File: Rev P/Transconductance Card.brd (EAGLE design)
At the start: 162.8 x 125.9 mm, 87 parts, among them IC1 74LS07D, IC10 ASSR-1530, IC12 LT1991MS, IC3 ISC0316-SMD, IC4 OP484, IC5 TLC272D, IC6 74LS00D, IC8 7438, IC9 ASSR-1530, Q1 IRF9Z24NPbF, Q2 2N7000, U1 MCP1700T-3302E/TT, X1 H15MLE

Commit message: Made bypass capacitor-diode thing symmetrical
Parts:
- added C44, C46: 1n, resistor:C1206
- added C45, C47: 0.1u, resistor:C1210
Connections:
- net GND: now also C44.2, C45.2, C46.2, C47.2
- net N$16: now also C44.1
- net N$22: now also C45.1
- net N$30: now also C46.1
- net N$32: now also C47.1
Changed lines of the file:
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@@
 <attribute name="VALUE" x="66.95" y="22.35" size="1.27" layer="27"/>
+</element>
+<element name="C44" library="resistor" package="C1206" value="1n" x="-20.32" y="-8.89" smashed="yes">
+<attribute name="NAME" x="-21.59" y="-7.62" size="1.27" layer="25"/>
+<attribute name="VALUE" x="-21.59" y="-11.43" size="1.27" layer="27"/>
+</element>
+<element name="C45" library="resistor" library_urn="urn:adsk.eagle:library:348" package="C1210" package3d_urn="urn:adsk.eagle:package:23619/2" value="0.1u" x="-20.32" y="-16.51" smashed="yes">
+<attribute name="NAME" x="-22.225" y="-14.605" size="1.27" layer="25"/>
+<attribute name="VALUE" x="-22.225" y="-19.685" size="1.27" layer="27"/>
+</element>
+<element name="C46" library="resistor" package="C1206" value="1n" x="-20.32" y="-24.13" smashed="yes">
+<attribute name="NAME" x="-21.59" y="-22.86" size="1.27" layer="25"/>
+<attribute name="VALUE" x="-21.59" y="-26.67" size="1.27" layer="27"/>
+</element>
+<element name="C47" library="resistor" library_urn="urn:adsk.eagle:library:348" package="C1210" package3d_urn="urn:adsk.eagle:package:23619/2" value="0.1u" x="-20.32" y="-31.75" smashed="yes">
+<attribute name="NAME" x="-22.225" y="-29.845" size="1.27" layer="25"/>
+<attribute name="VALUE" x="-22.225" y="-34.925" size="1.27" layer="27"/>
 </element>
 </elements>
@@
 <contactref element="U$1" pad="5"/>
 <contactref element="U$1" pad="4"/>
+<contactref element="C44" pad="2"/>
+<contactref element="C45" pad="2"/>
+<contactref element="C46" pad="2"/>
+<contactref element="C47" pad="2"/>
 <wire x1="129.54" y1="97.79" x2="135.89" y2="97.79" width="0" layer="19" extent="1-1"/>
 <wire x1="129.54" y1="93.98" x2="129.54" y2="97.79" width="0" layer="19" extent="1-1"/>
@@
 <wire x1="93.98" y1="87.63" x2="99.06" y2="90.17" width="0" layer="19" extent="1-1"/>
 <wire x1="88.9" y1="90.17" x2="93.98" y2="87.63" width="0" layer="19" extent="1-1"/>
+<wire x1="16.51" y1="18.415" x2="15.24" y2="11.43" width="0" layer="19" extent="1-1"/>
+<wire x1="19.685" y1="22.86" x2="16.51" y2="18.415" width="0" layer="19" extent="1-1"/>
+<wire x1="16.38" y1="27.94" x2="16.8275" y2="24.4475" width="0" layer="19" extent="1-1"/>
+<wire x1="24.13" y1="19.05" x2="19.685" y2="22.86" width="0" layer="19" extent="1-1"/>
 <wire x1="135.89" y1="90.17" x2="129.54" y2="93.98" width="0" layer="19" extent="1-1"/>
 <wire x1="135.89" y1="83.82" x2="135.89" y2="90.17" width="0" layer="19" extent="1-1"/>
@@
 <wire x1="125.4252" y1="56.1848" x2="130.5052" y2="61.2648" width="0" layer="19" extent="1-1"/>
 <wire x1="31.75" y1="8.89" x2="27.94" y2="2.54" width="0" layer="19" extent="1-1"/>
+<wire x1="25.53" y1="36.83" x2="19.3048" y2="32.7" width="0" layer="19" extent="1-1"/>
+<wire x1="26.67" y1="41.91" x2="25.4" y2="39.37" width="0" layer="19" extent="1-1"/>
+<wire x1="26.8" y1="31.75" x2="25.53" y2="36.83" width="0" layer="19" extent="1-1"/>
+<wire x1="34.29" y1="30.35" x2="29.21" y2="31.75" width="0" layer="19" extent="1-1"/>
+<wire x1="40.64" y1="36.7" x2="38.1" y2="30.35" width="0" layer="19" extent="1-1"/>
+<wire x1="46.99" y1="27.94" x2="46.99" y2="35.56" width="0" layer="19" extent="1-1"/>
 <wire x1="67.31" y1="1.5875" x2="59.69" y2="1.5875" width="0" layer="19" extent="1-1"/>
 <wire x1="73.66" y1="1.5875" x2="67.31" y2="1.5875" width="0" layer="19" extent="1-1"/>
@@
 <wire x1="136.525" y1="1.5875" x2="130.81" y2="1.5875" width="0" layer="19" extent="1-1"/>
 <wire x1="100.2" y1="8.89" x2="106.55" y2="8.89" width="0" layer="19" extent="1-1"/>
-<wire x1="16.51" y1="30.48" x2="8.89" y2="30.48" width="0" layer="19" extent="1-1"/>
-<wire x1="16.8275" y1="24.4475" x2="16.38" y2="27.94" width="0" layer="19" extent="1-1"/>
-<wire x1="24.13" y1="19.05" x2="19.685" y2="22.86" width="0" layer="19" extent="1-1"/>
-<wire x1="25.53" y1="36.83" x2="19.3048" y2="32.7" width="0" layer="19" extent="1-1"/>
-<wire x1="26.67" y1="41.91" x2="25.4" y2="39.37" width="0" layer="19" extent="1-1"/>
-<wire x1="26.8" y1="31.75" x2="25.53" y2="36.83" width="0" layer="19" extent="1-1"/>
-<wire x1="34.29" y1="30.35" x2="29.21" y2="31.75" width="0" layer="19" extent="1-1"/>
-<wire x1="40.64" y1="36.7" x2="38.1" y2="30.35" width="0" layer="19" extent="1-1"/>
-<wire x1="46.99" y1="27.94" x2="46.99" y2="35.56" width="0" layer="19" extent="1-1"/>
 <wire x1="120.65" y1="10.16" x2="112.9" y2="8.89" width="0" layer="19" extent="1-1"/>
 <wire x1="53.975" y1="39.37" x2="46.99" y2="35.56" width="0" layer="19" extent="1-1"/>
@@
 <wire x1="60.96" y1="29.21" x2="57.15" y2="33.655" width="0" layer="19" extent="1-1"/>
 <wire x1="66.04" y1="27.94" x2="60.96" y2="29.21" width="0" layer="19" extent="1-1"/>
+<wire x1="67.65" y1="24.9" x2="66.04" y2="27.94" width="0" layer="19" extent="1-1"/>
+<wire x1="67.65" y1="24.4" x2="67.65" y2="24.9" width="0" layer="19" extent="1-1"/>
 <wire x1="69.85" y1="30.48" x2="66.04" y2="27.94" width="0" layer="19" extent="1-1"/>
 <wire x1="72.26" y1="34.29" x2="72.26" y2="30.48" width="0" layer="19" extent="1-1"/>
@@
 <wire x1="86.36" y1="27.94" x2="81.28" y2="26.67" width="0" layer="19" extent="1-1"/>
 <wire x1="93.98" y1="24.13" x2="88.9" y2="27.81" width="0" layer="19" extent="1-1"/>
+<wire x1="66.04" y1="15.24" x2="67.65" y2="24.4" width="0" layer="19" extent="1-1"/>
 <wire x1="104.14" y1="31.75" x2="97.79" y2="24.13" width="0" layer="19" extent="1-1"/>
 <wire x1="109.22" y1="30.48" x2="104.14" y2="31.75" width="0" layer="19" extent="1-1"/>
@@
 <wire x1="33.02" y1="67.31" x2="29.21" y2="64.9" width="0" layer="19" extent="1-1"/>
 <wire x1="41.91" y1="64.77" x2="33.02" y2="67.31" width="0" layer="19" extent="1-1"/>
-<wire x1="66.04" y1="15.24" x2="76.2" y2="13.97" width="0" layer="19" extent="1-1"/>
 <wire x1="53.34" y1="64.77" x2="41.91" y2="64.77" width="0" layer="19" extent="1-1"/>
 <wire x1="54.61" y1="54.61" x2="53.34" y2="64.77" width="0" layer="19" extent="1-1"/>
@@
 <wire x1="77.47" y1="54.61" x2="68.58" y2="54.74" width="0" layer="19" extent="1-1"/>
 <wire x1="76.1873" y1="73.152" x2="68.58" y2="64.77" width="0" layer="19" extent="1-1"/>
-<wire x1="16.51" y1="18.415" x2="2.54" y2="8.89" width="0" layer="19" extent="1-1"/>
-<wire x1="67.65" y1="24.9" x2="16.51" y2="18.415" width="0" layer="19" extent="1-1"/>
-<wire x1="67.65" y1="24.4" x2="67.65" y2="24.9" width="0" layer="19" extent="1-1"/>
+<wire x1="-18.92" y1="-8.89" x2="2.54" y2="8.89" width="0" layer="19" extent="1-1"/>
+<wire x1="-18.92" y1="-16.51" x2="-18.92" y2="-8.89" width="0" layer="19" extent="1-1"/>
+<wire x1="-18.92" y1="-24.13" x2="-18.92" y2="-16.51" width="0" layer="19" extent="1-1"/>
+<wire x1="-18.92" y1="-31.75" x2="-18.92" y2="-24.13" width="0" layer="19" extent="1-1"/>
 </signal>
 <signal name="+5V">
@@
 <wire x1="117.79" y1="88.73" x2="119.38" y2="90.32" width="1.016" layer="1"/>
 <wire x1="119.38" y1="90.32" x2="119.38" y2="91.31" width="1.016" layer="1"/>
+<contactref element="C44" pad="1"/>
+<wire x1="-21.72" y1="-8.89" x2="117.79" y2="88.73" width="0" layer="19" extent="1-1"/>
 </signal>
 <signal name="N$22">
@@
 <wire x1="115.89" y1="88.73" x2="115.57" y2="89.05" width="1.016" layer="1"/>
 <wire x1="115.57" y1="89.05" x2="115.57" y2="91.31" width="1.016" layer="1"/>
+<contactref element="C45" pad="1"/>
+<wire x1="-21.72" y1="-16.51" x2="115.89" y2="88.73" width="0" layer="19" extent="1-1"/>
 </signal>
 <signal name="N$30">
@@
 <wire x1="115.89" y1="76.37" x2="115.57" y2="76.05" width="1.016" layer="1"/>
 <wire x1="115.57" y1="76.05" x2="115.57" y2="73.79" width="1.016" layer="1"/>
+<contactref element="C46" pad="1"/>
+<wire x1="-21.72" y1="-24.13" x2="115.57" y2="73.79" width="0" layer="19" extent="1-1"/>
 </signal>
 <signal name="N$32">
@@
 <wire x1="117.79" y1="76.37" x2="119.38" y2="74.78" width="1.016" layer="1"/>
 <wire x1="119.38" y1="74.78" x2="119.38" y2="73.79" width="1.016" layer="1"/>
+<contactref element="C47" pad="1"/>
+<wire x1="-21.72" y1="-31.75" x2="119.38" y2="73.79" width="0" layer="19" extent="1-1"/>
 </signal>
 <signal name="N$33">

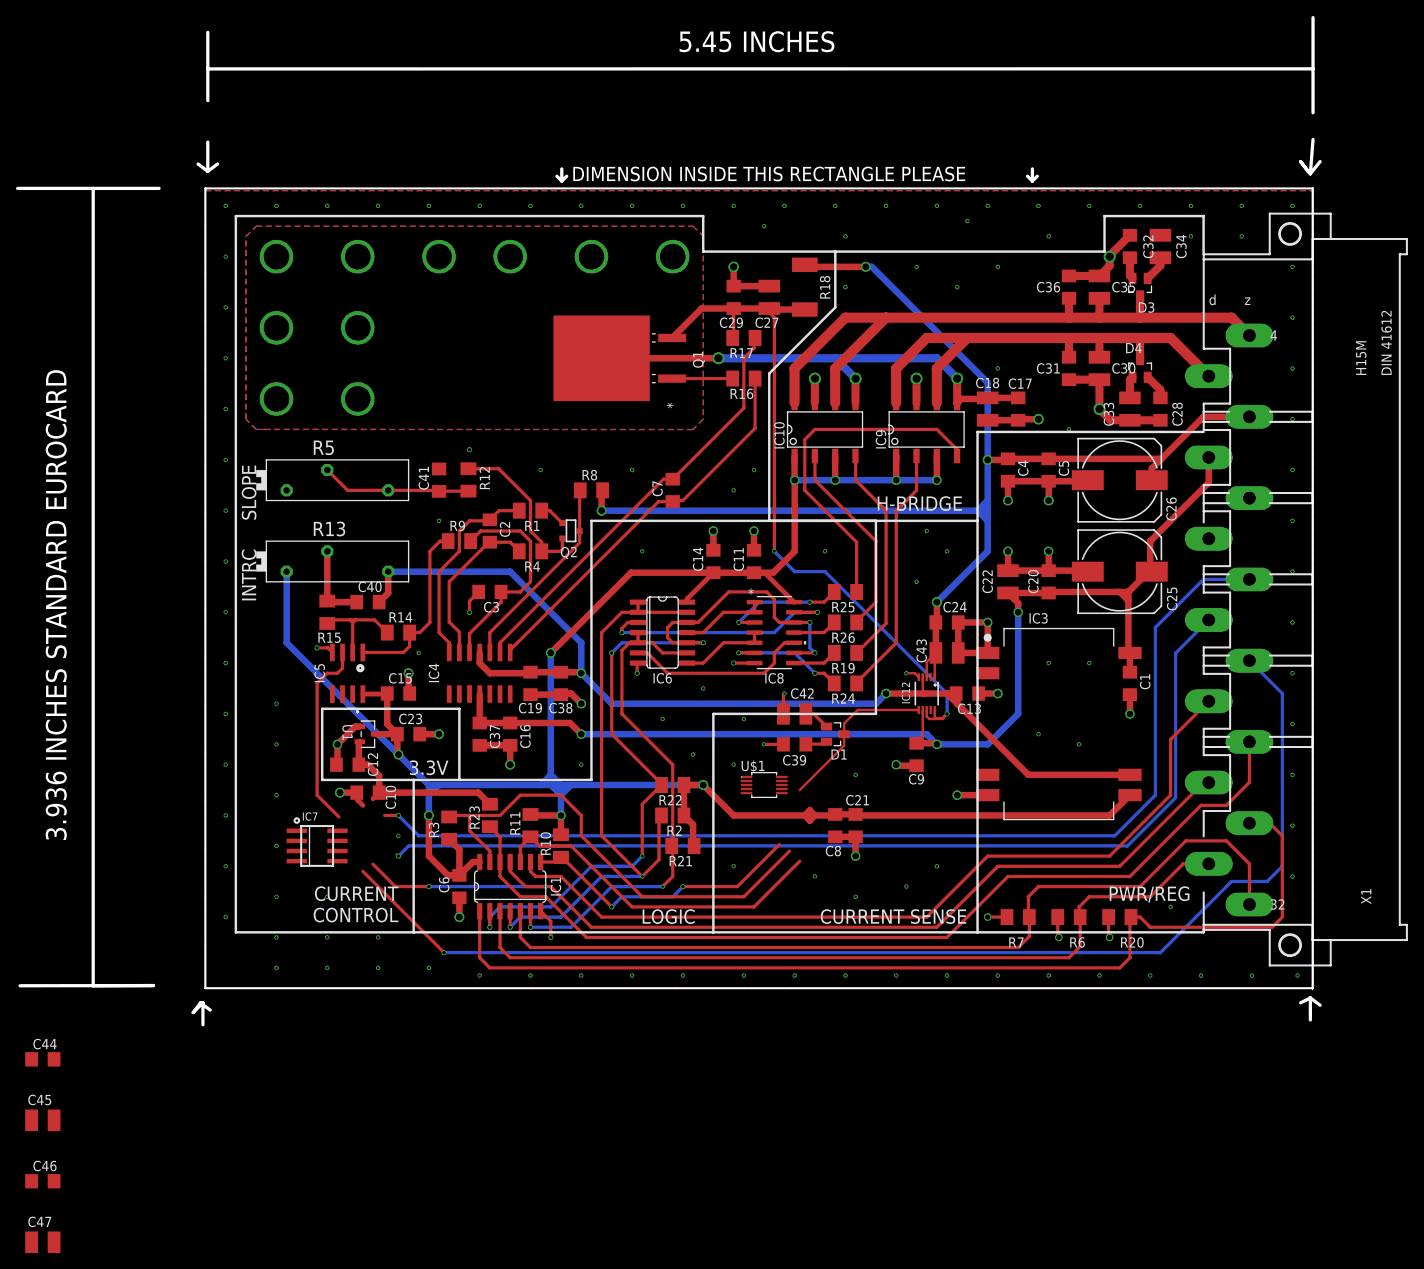
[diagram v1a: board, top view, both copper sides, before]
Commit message: Partial Board Routing
Need to finish routing power and update schematic power/GND symbols to be consistent with new convention
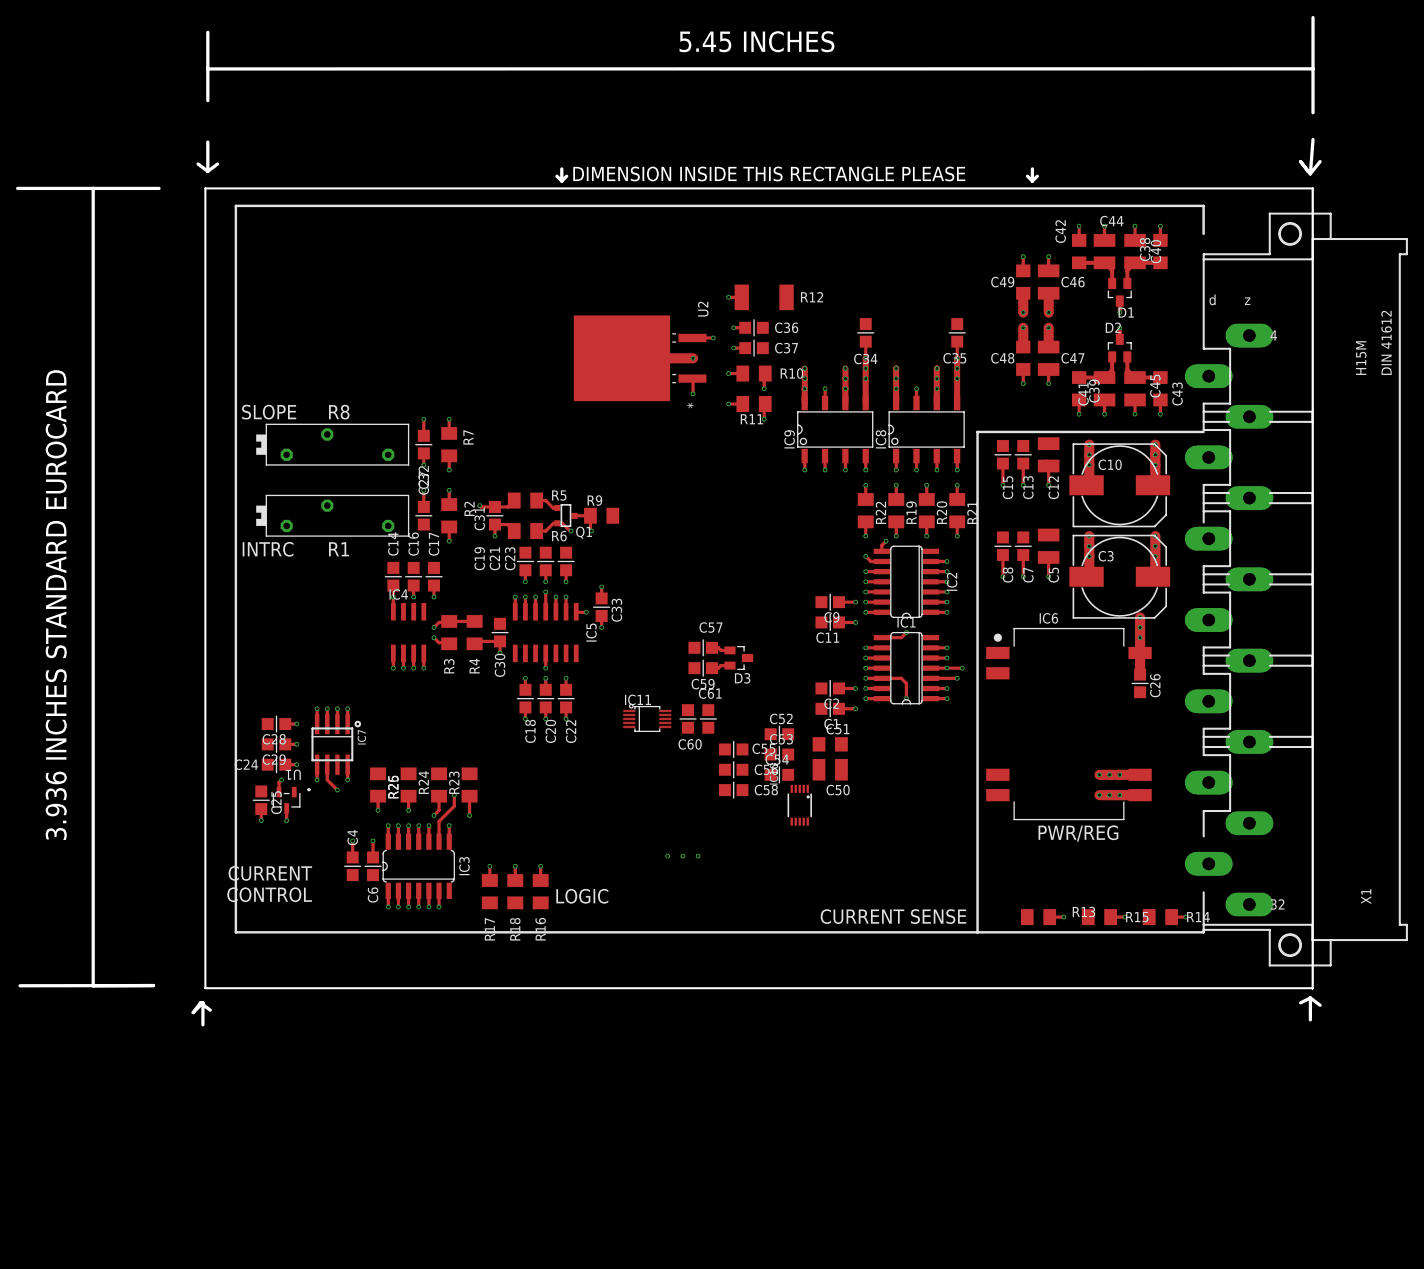
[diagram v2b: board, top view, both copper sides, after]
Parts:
- removed D4: BAS70-04, diode:SOT23
- removed IC12: LT1991MS, linear-technology:MSOP10
- removed Q2: 2N7000, UL_2N7002:SOT-23
- removed U$1: ADS8319, MeRCIS Lab Parts:VSSOP-10
- added C48, C49, C51: 1n, resistor:C1206
- added C50: 0.1u, resistor:C1210
- added C52, C55, C60: 1u, MeRCIS Lab Parts:C0805
- added C53, C56, C57, C61: 0.1u, MeRCIS Lab Parts:C0805
- added C54, C58: 0.01u, MeRCIS Lab Parts:C0805
- added C59: 1n, MeRCIS Lab Parts:C0805
- added D2: BAS70-04, diode:SOT23
- added IC11: ADS8319, MeRCIS Lab Parts:VSSOP-10
- added IC2: 74LS00, MeRCIS Lab Parts:74XX-US_SO14:1
- added U2: IRF9Z24NPbF, UL_IRF9Z24:D2PAK
- C1, C19: value 0.1u -> 1u; device resistor:C1206 -> MeRCIS Lab Parts:C0805
- C10, C3: value 0.1u -> 470u; device resistor:C1206 -> rcl:140CLH-1010
- C11, C14, C16, C20, C4: device resistor:C1206 -> MeRCIS Lab Parts:C0805
- C12: value 1u -> 10u; device resistor:C1206 -> resistor:C1210
- C13, C7, C9: value 0.01u -> 1u; device resistor:C1206 -> MeRCIS Lab Parts:C0805
- C15, C2, C21, C6: value 0.01u -> 0.1u; device resistor:C1206 -> MeRCIS Lab Parts:C0805
- C17, C24: value 1n -> 1u; device resistor:C1206 -> MeRCIS Lab Parts:C0805
- C18: value 0.1u -> 1u; device resistor:C1210 -> MeRCIS Lab Parts:C0805
- C22: value 10u -> 0.01u; device resistor:C1210 -> MeRCIS Lab Parts:C0805
- C23: value 1u -> 0.01u; device resistor:C1206 -> MeRCIS Lab Parts:C0805
- C25: value 470u -> 1u; device resistor1:153CLV-1010 -> MeRCIS Lab Parts:C0805
- C26: value 470u -> 0.1u; device resistor1:153CLV-1010 -> MeRCIS Lab Parts:C0805
- C27, C30, C34: device resistor:C1210 -> MeRCIS Lab Parts:C0805
- C28, C32, C36: value 1n -> 0.1u; device resistor:C1206 -> MeRCIS Lab Parts:C0805
- C29: value 1n -> 10u; device resistor:C1206 -> MeRCIS Lab Parts:C0805
- C31: value 1n -> 0.01u; device resistor:C1206 -> MeRCIS Lab Parts:C0805
- C33: value 0.1u -> 0.01u; device resistor:C1210 -> MeRCIS Lab Parts:C0805
- C35: value 0.1u -> 1n; device resistor:C1210 -> MeRCIS Lab Parts:C0805
- C37: value 0.01u -> 1n; device resistor:C1206 -> MeRCIS Lab Parts:C0805
- C38: value 0.01u -> 1n
- C40, C41: device resistor:C1206 -> resistor:C1210
- C42, C43: value 0.1u -> 1n; device resistor:C1210 -> resistor:C1206
- C44, C46: value 1n -> 0.1u; device resistor:C1206 -> resistor:C1210
- C5: value 0.1u -> 10u; device resistor:C1206 -> resistor:C1210
- C8: value 1u -> 0.1u; device resistor:C1206 -> MeRCIS Lab Parts:C0805
- IC1: value 74LS07D -> 74LS00; device 74xx-eu:SO14 -> MeRCIS Lab Parts:74XX-US_SO14:1
- IC10: value ASSR-1530 -> LT1991MS; device ASSR-1530:SO8 -> linear-technology:MSOP10
- IC3: value ISC0316-SMD -> 74LS07D; device SF_ISC03:SOP254P1879X863-16N -> 74xx-eu:SO14
- IC4: value OP484 -> TLC272D; device linear:SO14 -> linear:SO08
- IC5: value TLC272D -> OP484; device linear:SO08 -> linear:SO14
- IC6: value 74LS00D -> SF_ISC03_DC_DC16-SMD; device 74xx-us:SO14 -> MeRCIS Lab Parts:SF_ISC03_SOP254P1879X863-16N
- IC8: value 7438 -> ASSR-1530; device SN7438:D14 -> MeRCIS Lab Parts:ASSR-1530_SO8
- IC9: device ASSR-1530:SO8 -> MeRCIS Lab Parts:ASSR-1530_SO8
- Q1: value IRF9Z24NPbF -> 2N7000; device UL_IRF9Z24:D2PAK -> UL_2N7002:SOT-23
- R1: value 100ohm -> 20k; device resistor:M1206 -> rcl:PT-SPIN
- R10, R25: value 330 -> 1k
- R11: value 330 -> 100ohm
- R12: value 9.1k -> 1ohm; device resistor:M1206 -> resistor:R2512
- R13: value 20k -> 10k; device rcl:PT-SPIN -> resistor:M1206
- R14: value 220 -> 10k
- R15: value 100k -> 10k
- R16: value 100ohm -> 10k
- R17: value 1k -> 10k
- R18: value 1ohm -> 10k; device resistor:R2512 -> resistor:M1206
- R2: value 10k -> 100k
- R20, R21, R22: value 10k -> 330
- R23: value 2k -> 330
- R26: value 330 -> 2k
- R3: value 1k -> 220
- R5: value 5k -> 100ohm; device rcl:PT-SPIN -> resistor:M1206
- R6: value 10k -> 1k
- R7: value 10k -> 9.1k
- R8: value 1k -> 5k; device resistor:M1206 -> rcl:PT-SPIN
- moved C46 168.6 mm to (105.4, 88.3), turned to 90 degrees
- moved C47 167.4 mm to (105.4, 78.7), turned to 270 degrees
- moved C44 166.8 mm to (112.4, 92.1), turned to 90 degrees
- moved C45 164.3 mm to (116.2, 74.9), turned to 270 degrees
- moved C28 117.3 mm to (8.89, 33.0), turned to 180 degrees
- moved C25 111.1 mm to (6.99, 23.5), turned to 90 degrees
- moved C40 105.4 mm to (116.2, 92.1), turned to 90 degrees
- moved R15 103.8 mm to (111.8, 8.89), turned to 0 degrees
- moved R14 101.7 mm to (119.4, 8.89)
- moved C10 101.5 mm to (114.3, 62.9), turned to 0 degrees
- moved R13 98.3 mm to (104.1, 8.89)
- moved C12 95.8 mm to (105.4, 66.7), turned to 90 degrees
- moved C4 95.7 mm to (18.4, 15.2)
- moved R7 92.4 mm to (30.5, 67.9), turned to 270 degrees
- moved C38 92.3 mm to (119.4, 92.1)
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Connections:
- removed net N$12: IC4.10, Q2.3, R8.1
- removed net N$35: IC7.P$2
- removed net N$36: IC7.P$8
- new net +3.3V: C24.1, C28.1, C29.1, IC7.P$3, IC7.P$8, U1.2
- new net AGND: C10.-, C12.2, C13.2, C14.2, C15.2, C16.2, C17.2, C18.2, C19.1, C20.2, C21.1, C22.2, C23.1, C26.2, C3.-, C30.2, C32.2, C5.2, C7.2, C8.2, IC4.4, IC7.P$2, R8.1
- new net DGND: C1.2, C11.2, C2.2, C24.2, C25.2, C28.2, C29.2, C4.2, C6.2, C9.2, IC1.7, IC2.7, IC3.7, IC6.1, IC6.8, IC7.P$7, R13.1, R14.1, R15.1, U1.1
- new net N$37: IC4.2, R2.2, R3.1
- new net VDD: C1.1, C11.1, C2.1, C9.1, IC1.14, IC2.14
- net +20V: now also C10.+, C12.1, C13.1, C15.1, C50.1, C51.1, IC10.1, IC10.3, R12.2, R9.2; no longer C24.1, C26.+, C4.1, C43.1, C5.1, IC12.1, IC12.3, R18.2, R8.2
- net +24V: now also C18.1, C26.1, C3.+, C5.1, C55.1, C56.1, C58.1, C7.1, C8.1, IC10.7, IC5.4, IC6.16; no longer C1.1, C16.1, C25.+, C37.1, C9.1, IC12.7, IC3.16, IC4.4
- net +3V3: now also R26.1; no longer C10.1, C12.1, IC7.P$3, R23.1, U1.2
- net +5V: now also C16.1, C17.1, C25.1, C4.1, C60.1, C61.1, IC11.1, IC11.10, IC11.2, IC11.9, IC3.14, IC4.8, IC6.9, IC8.1, IC8.3, R1.1, R16.1, R17.1, R18.1, R23.2, R24.2, R25.1; no longer C11.1, C15.1, C21.1, C23.1, C8.1, IC1.14, IC10.1, IC10.3, IC3.9, IC5.8, IC6.14, IC8.14, R10.2, R11.2, R13.1, R2.1, R21.1, R22.1, R3.1, U$1.1, U$1.10, U$1.2, U$1.9
- net -5V: now also C21.2, C23.2, C27.2, C52.2, C53.2, C54.2, IC10.4, IC5.11, IC6.10, R1.2; no longer C13.2, C38.2, C40.2, IC12.4, IC3.10, IC4.11, R13.2
- net 1: now also IC1.4, IC1.5, IC1.9, IC3.6, R17.2; no longer IC1.6, IC6.4, IC6.5, IC6.9, R21.2
- net 2: now also IC1.1, IC1.13, IC1.2, IC3.4, R18.2; no longer IC1.4, IC6.1, IC6.13, IC6.2, R2.2
- net 3: now also IC1.10, IC1.12, IC2.12, IC2.9, IC3.2, R16.2; no longer IC1.2, IC6.10, IC6.12, IC8.12, IC8.9, R22.2
- net 3&1: now also IC8.2, R20.1; no longer IC9.2, R24.1
- net 3&2: now also IC8.4, R21.1; no longer IC9.4, R25.1
- net ADC-CS: now also IC3.9; no longer IC1.9
- net CLK: now also IC3.11; no longer IC1.11
- net GND: now also C38.2, C40.2, C48.2, C49.2, C50.2, C51.2, C52.1, C53.1, C54.1, C55.2, C56.2, C57.2, C58.2, C59.2, C60.2, C61.2, IC10.5, IC11.4, IC11.5; no longer C1.2, C10.2, C11.2, C12.2, C13.1, C14.2, C15.2, C16.2, C17.2, C18.2, C19.1, C20.2, C21.2, C22.2, C23.2, C24.2, C25.-, C26.-, C27.2, C28.2, C29.2, C3.2, C30.2, C31.2, C32.2, C33.2, C38.1, C4.2, C5.2, C6.2, C8.2, C9.2, IC1.7, IC10.7, IC12.5, IC3.1, IC3.8, IC5.4, IC6.7, IC7.P$7, R20.1, R5.1, R6.1, R7.1, U$1.4, U$1.5, U1.1
- net H-BDG: now also C34.1, C35.1, IC8.5, U2.2; no longer C17.1, C18.1, IC10.5, Q1.2
- net H-EN: now also IC3.1, R13.2; no longer IC1.1, R20.2
- net H-NEG: now also IC3.3, R15.2; no longer IC1.3, R6.2
- net H-POS: now also IC3.5, R14.2; no longer IC1.5, R7.2
- net LOAD_N: now also C47.1, C48.1, D2.3, IC8.6, IC8.8; no longer C30.1, C31.1, D4.3, IC9.6, IC9.8
- net LOAD_P: now also C46.1, C49.1, D1.3, IC9.6, IC9.8; no longer C35.1, C36.1, D3.3, IC10.6, IC10.8
- net LSENSE: now also C36.1, C37.1, IC10.10, IC10.8, R10.2, R12.1, U2.3; no longer C27.1, C29.1, IC12.10, IC12.8, Q1.3, R17.2, R18.1
- net MISO: now also IC3.12, R26.2; no longer IC1.12, R23.2
- net N$1: now also D3.3, IC10.6, IC11.3; no longer D1.3, IC12.6, U$1.3
- net N$10: now also IC4.3; no longer IC5.3
- net N$11: now also IC5.10, Q1.3, R9.1; no longer Q2.2, R12.2, R4.1
- net N$13: now also R11.2, U2.1; no longer Q1.1, R16.2
- net N$14: now also C31.2, IC5.13, R6.2; no longer C2.2, IC4.13, R4.2
- net N$15: now also C33.2, IC5.8, R11.1; no longer C7.2, IC4.8, R16.1
- net N$16: now also C38.1, C40.1, D1.1; no longer C34.1, C44.1, D3.1
- net N$17: now also C30.1, IC5.12, R4.2; no longer C3.1, IC4.12, R9.2
- net N$18: now also C32.1, R7.1, R8.2, R8.3; no longer C41.1, R12.1, R5.2, R5.3
- net N$2: now also Q1.2, R6.1, R7.2; no longer IC5.2, R14.1, R15.2
- net N$20: now also C33.1, IC5.9, R10.1; no longer C7.1, IC4.9, R17.1
- net N$21: now also C27.1, R1.3, R2.1; no longer C40.1, R13.3, R15.1
- net N$22: now also C42.1, C44.1, D1.2; no longer C32.1, C45.1, D3.2
- net N$23: now also IC1.8, IC2.4, IC2.5; no longer IC6.8, IC8.4, IC8.5
- net N$24: now also IC1.11, IC2.1, IC2.2; no longer IC6.11, IC8.1, IC8.2
- net N$25: now also IC2.8; no longer IC8.8
- net N$26: now also IC2.6, R20.2; no longer IC8.6, R24.2
- net N$27: now also IC2.3, R21.2; no longer IC8.3, R25.2
- net N$28: now also IC4.1, R3.2, R4.1; no longer IC5.1, R14.2, R9.1
- net N$29: now also IC2.11, R22.2; no longer IC8.11, R26.2
- net N$3: now also IC11.6, IC3.8, R23.1; no longer IC1.8, R10.1, U$1.6
- net N$30: now also C39.1, C41.1, D2.1; no longer C33.1, C46.1, D4.1
- net N$32: now also C43.1, C45.1, D2.2; no longer C28.1, C47.1, D4.2
- net N$33: now also C57.1, D3.1; no longer C42.1, D1.1
- net N$34: now also C59.1, D3.2; no longer C39.1, D1.2
- net N$4: now also IC11.8, IC3.10, R24.1; no longer IC1.10, R11.1, U$1.8
- net N$5: now also Q1.1, R5.1; no longer Q2.1, R1.1
- net N$6: now also IC1.6, IC2.10; no longer IC6.6, IC8.10
- net N$7: now also IC1.3, IC2.13; no longer IC6.3, IC8.13
- net N$8: now also IC11.7, IC3.13, R25.2; no longer IC1.13, R3.2, U$1.7
- net N$9: now also C31.1, IC5.14, R5.2; no longer C2.1, IC4.14, R1.2
- net ~3||1: now also IC9.4; no longer IC10.4
- net ~3||2: now also IC9.2, R22.1; no longer IC10.2, R26.1
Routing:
- net +5V: track 297.4 -> 41.6 mm, vias 9 -> 15
- net GND: track 169.3 -> 24.9 mm, vias 157 -> 14
- net LDAC: track 134.7 -> 0.00 mm, vias 1 -> 0
- net +20V: track 164.5 -> 49.3 mm, vias 4 -> 6
- net -5V: track 130.1 -> 19.3 mm, vias 2 -> 7
- net +24V: track 144.3 -> 77.7 mm, vias 3 -> 13
- net LSENSE: track 88.8 -> 26.2 mm, vias 2 -> 5
- net 1: track 63.8 -> 117.5 mm, vias 2 -> 7
- net N$8: track 59.7 -> 7.48 mm, vias 0 -> 2
- net 3&2: track 43.2 -> 5.44 mm, vias 0 -> 2
- net N$4: track 43.3 -> 6.21 mm, vias 0 -> 2
- net 2: track 75.4 -> 112.0 mm, vias 2 -> 6
- net +3.3V: track 0.00 -> 35.8 mm, vias 0 -> 6
- net 3: track 101.6 -> 136.1 mm, vias 6 -> 8
- net N$3: track 39.0 -> 7.48 mm
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- removed copper zone on layer 1, net GND
- removed copper zone on layer 16, net GND
- removed copper zone on layer 2, net GND
- removed copper zone on layer 3, net GND
- removed copper zone on layer 1, net H-BDG
- removed copper zone on layer 16, net H-BDG
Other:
- board text added: "Copyright 2021, Matthew Gaines, MeRCIS LABS, CWRU"
- board text added: "Revision P Joseph Cressman, Matthew Gaines Sung Yoon Jung, Julian Narvaez, Hangxing Liu, David Lituchy, Samuel Xu, Mac Russell, & Reinhardt G. "KAM" CRISS MeRCIS LABS Case Western Reserve University"
- board text removed: "3.3V"
- board text removed: "Copyright 2020, Sung Yoon Jung, MeRCIS LABS, CWRU"
- board text removed: "H-BRIDGE"
- board text removed: "Revision O.2 Joseph Cressman, Matthew Gaines Sung Yoon Jung, Julian Narvaez, Hangxing Liu, David Lituchy, Samuel Xu, Mac Russell, & Reinhardt G. "KAM" CRISS MeRCIS LABS Case Western Reserve University"
- board text removed: "Transconductance Card,REV O.2"
